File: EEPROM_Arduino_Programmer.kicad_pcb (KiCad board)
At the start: 2 copper layers, 40.4 x 52.8 mm, 4 parts, among them U1 74HC595, U2 74HC595, U3 28C16_EEPROM

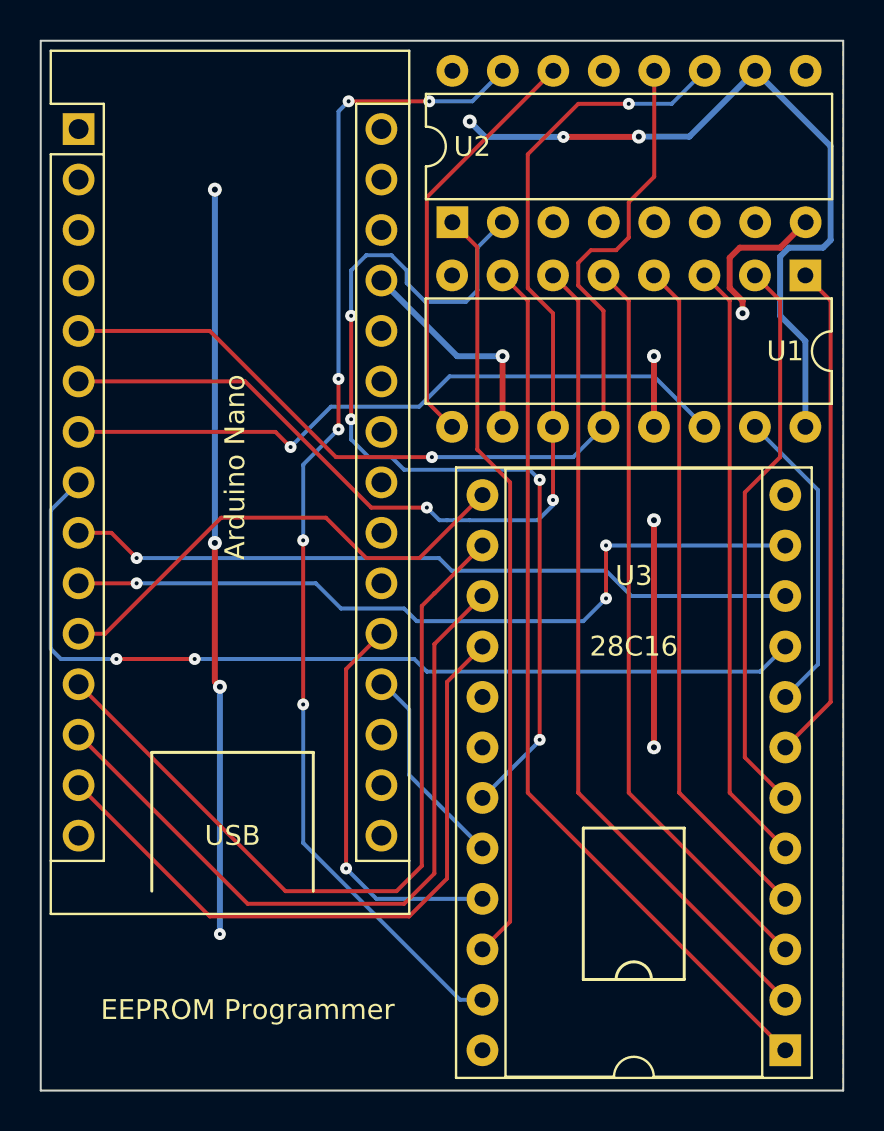
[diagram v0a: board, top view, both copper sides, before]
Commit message: updated kicad version from 7 to 9!
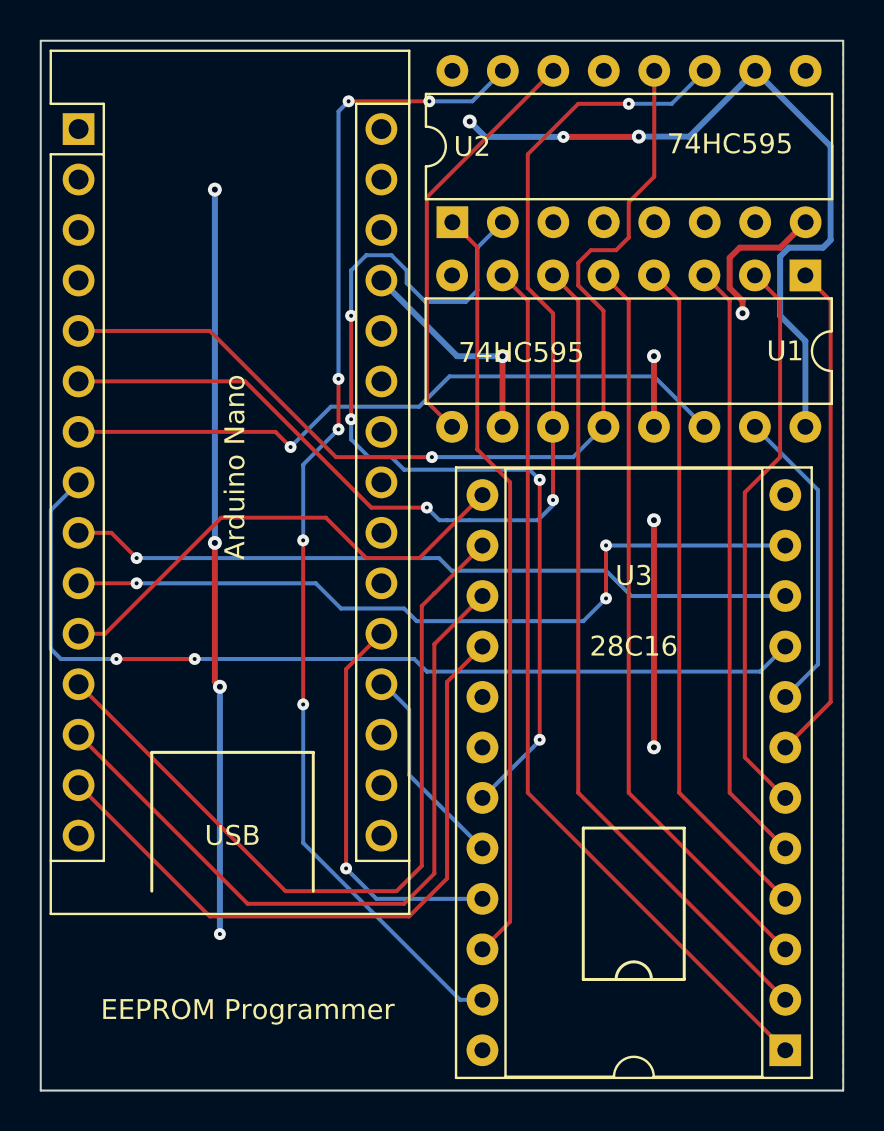
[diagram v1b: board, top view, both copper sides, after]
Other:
- board text added: "74HC595"
